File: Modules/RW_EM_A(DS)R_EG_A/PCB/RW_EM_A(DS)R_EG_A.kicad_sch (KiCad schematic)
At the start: 50 parts, among them J1 PJ301M-12, J2 IDC_02x05, J3 PJ301M-12, J4 PJ301M-12, Q1 BC548, SW1 SW_SPDT, U1 TL072, U2 TL074

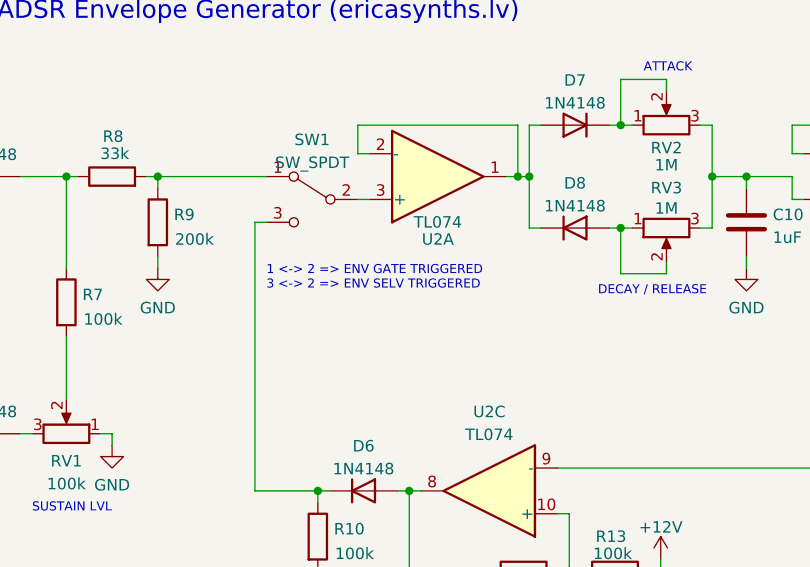
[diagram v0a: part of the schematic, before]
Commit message: Updated all schematics with link to repo. Also updated all readme files
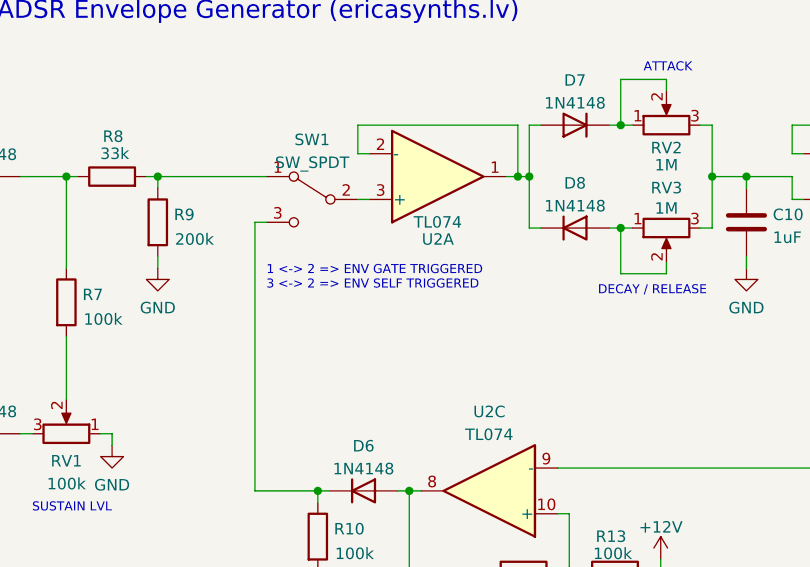
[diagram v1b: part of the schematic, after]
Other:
- note added: "1 <-> 2 => ENV GATE TRIGGERED 3 <-> 2 => ENV SELF TRIGGERED"
- note removed: "1 <-> 2 => ENV GATE TRIGGERED 3 <-> 2 => ENV SELV TRIGGERED"
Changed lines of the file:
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@@
     (rev "2022-10-19")
     (comment 1 "Licensed under CERN-OHL-S v2+")
+    (comment 2 "https://github.com/sunfl0w/RW_EM")
   )
   (junction (at 224.79 101.6) (diameter 0) (color 0 0 0 0)
@@
     (effects (font (size 1 1)) (justify left bottom))
   )
-  (text "1 <-> 2 => ENV GATE TRIGGERED\n3 <-> 2 => ENV SELV TRIGGERED"
+  (text "1 <-> 2 => ENV GATE TRIGGERED\n3 <-> 2 => ENV SELF TRIGGERED"
     (at 138.43 99.06 0)
     (effects (font (size 1 1)) (justify left bottom))
